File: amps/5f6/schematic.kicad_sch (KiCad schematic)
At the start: 69 parts, among them T3 2R sec

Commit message: Fix: the drawn tone stacks now are the tone stack the lab plots, and a gate says so
The tone-stack lab solves one network — the FMV stack documented in
site/src/lib/tonestack.js — and fills its values from each amp's BOM by
reference designator. Nothing checked that the schematic drew those
designators into that network, and nine of the nine drawings did not.

What the drawings said, rebuilt from the committed .kicad_sch files rather
than from the generators:

- 5F6-A, JTM45, 1987, 1959 and 5F4 ran the treble capacitor off the slope
  resistor's FOOT instead of the stack input, and landed the treble pot's
  lower lug on the bass-capacitor node instead of the slope foot.
- Every three-knob drawing left the bass pot's wiper unwired, so the plotted
  output (treble wiper AND bass wiper) existed on no drawing.
- JTM45, 1987 and 1959 put the mid capacitor in series with the mid pot down
  to ground rather than from the slope foot to the mid leg's top.
- 5F6 tied its bass pot as a rheostat and fed the mid capacitor to the middle
  pot's wiper.
- The blackface circuits left the treble pot's lower lug on the bass-cap node
  and tied the bass wiper to its own lug; AB763 drew its 0.047 µF inline on
  top of the bass pot's lug.

The 5F6-A's own layout.yaml — redrawn from the published Fender 5F6-A layout
sheet — already wires the canonical network (treble low to the slope node,
both wipers to the phase-inverter coupler), and 5F4's does too, so the
drawings were corrected to that rather than the lab to the drawings.

Consequences beyond the wires:

- 5F6-A's parts list prints one 0.02 µF line covering the bass and middle
  positions; the drawing showed one capacitor where the circuit has two.
  Added C5b with the same value and the same printed line cited. The plotted
  curve does not move — both positions already used that value.
- The blackface stacks keep the capacitor that feeds the mid leg. With the
  lug corrected, CBN/CB1 (0.1 µF) feeds the bass pot and CBN2/CB2 (0.047 µ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
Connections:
- net at VR4.3, VR5.1: now also C7.2, VR5.2 (W)
- net at C6.2, VR4.1: no longer VR3.3, VR4.2 (W)
- net at C6.1, C7.1, RSL.2: now also VR3.3
- net at C10.1, VR3.2 (W): now also VR4.2 (W)
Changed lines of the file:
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@@
   (wire (pts (xy 116.84 119.5) (xy 124.46 119.5))
+    (stroke (width 0) (type default)))
+  (junction (at 124.46 119.5) (diameter 0) (color 0 0 0 0))
+  (wire (pts (xy 124.46 119.5) (xy 124.46 94))
+    (stroke (width 0) (type default)))
+  (wire (pts (xy 124.46 94) (xy 140.19 94))
     (stroke (width 0) (type default)))
   (symbol (lib_id "cx:R") (at 128.27 119.5 90) (unit 1)
@@
     (property "Value" "56k" (at 125.07 115.9 270) (effects (font (size 1.27 1.27)) (justify left))))
   (wire (pts (xy 132.08 119.5) (xy 137 119.5))
-    (stroke (width 0) (type default)))
-  (junction (at 121 119.5) (diameter 0) (color 0 0 0 0))
-  (wire (pts (xy 121 119.5) (xy 121 94))
-    (stroke (width 0) (type default)))
-  (wire (pts (xy 121 94) (xy 140.19 94))
     (stroke (width 0) (type default)))
   (symbol (lib_id "cx:C") (at 144 94 90) (unit 1)
@@
     (property "Reference" "VR3" (at 154.6 94.61 0) (effects (font (size 1.27 1.27)) (justify left)))
     (property "Value" "250k treb" (at 154.6 97.01 0) (effects (font (size 1.27 1.27)) (justify left))))
-  (junction (at 137 119.5) (diameter 0) (color 0 0 0 0))
-  (wire (pts (xy 137 119.5) (xy 137 104))
+  (wire (pts (xy 137 119.5) (xy 137 101.62))
     (stroke (width 0) (type default)))
-  (symbol (lib_id "cx:C") (at 144 104 90) (unit 1)
+  (wire (pts (xy 137 101.62) (xy 152.4 101.62))
+    (stroke (width 0) (type default)))
+  (junction (at 137 106) (diameter 0) (color 0 0 0 0))
+  (junction (at 137 118) (diameter 0) (color 0 0 0 0))
+  (symbol (lib_id "cx:C") (at 144 106 90) (unit 1)
     (in_bom yes) (on_board yes)
-    (property "Reference" "C6" (at 140.8 97.8 270) (effects (font (size 1.27 1.27)) (justify left)))
-    (property "Value" ".02u" (at 140.8 100.2 270) (effects (font (size 1.27 1.27)) (justify left))))
-  (wire (pts (xy 137 104) (xy 140.19 104))
+    (property "Reference" "C6" (at 140.8 99.8 270) (effects (font (size 1.27 1.27)) (justify left)))
+    (property "Value" ".02u" (at 140.8 102.2 270) (effects (font (size 1.27 1.27)) (justify left))))
+  (wire (pts (xy 137 106) (xy 140.19 106))
     (stroke (width 0) (type default)))
-  (wire (pts (xy 147.81 104) (xy 152.4 104))
+  (wire (pts (xy 147.81 106) (xy 152.4 106))
     (stroke (width 0) (type default)))
-  (junction (at 152.4 104) (diameter 0) (color 0 0 0 0))
-  (wire (pts (xy 137 119.5) (xy 137 143))
+  (symbol (lib_id "cx:C") (at 144 118 90) (unit 1)
+    (in_bom yes) (on_board yes)
+    (property "Reference" "C7" (at 140.8 111.8 270) (effects (font (size 1.27 1.27)) (justify left)))
+    (property "Value" ".02u" (at 140.8 114.2 270) (effects (font (size 1.27 1.27)) (justify left))))
+  (wire (pts (xy 137 118) (xy 140.19 118))
     (stroke (width 0) (type default)))
-  (symbol (lib_id "cx:C") (at 144 143 90) (unit 1)
-    (in_bom yes) (on_board yes)
-    (property "Reference" "C7" (at 140.8 136.8 270) (effects (font (size 1.27 1.27)) (justify left)))
-    (property "Value" ".02u" (at 140.8 139.2 270) (effects (font (size 1.27 1.27)) (justify left))))
-  (wire (pts (xy 137 143) (xy 140.19 143))
-    (stroke (width 0) (type default)))
-  (wire (pts (xy 147.81 143) (xy 161 143))
-    (stroke (width 0) (type default)))
-  (wire (pts (xy 161 143) (xy 161 121.81))
-    (stroke (width 0) (type default)))
-  (wire (pts (xy 161 121.81) (xy 157.48 121.81))
-    (stroke (width 0) (type default)))
-  (wire (pts (xy 152.4 101.62) (xy 152.4 106))
+  (wire (pts (xy 147.81 118) (xy 152.4 118))
     (stroke (width 0) (type default)))
   (symbol (lib_id "cx:POT") (at 152.4 109.81 0) (unit 1)
@@
     (property "Reference" "VR4" (at 154.6 106.61 0) (effects (font (size 1.27 1.27)) (justify left)))
     (property "Value" "1M bass" (at 154.6 109.01 0) (effects (font (size 1.27 1.27)) (justify left))))
-  (wire (pts (xy 157.48 109.81) (xy 166 109.81))
-    (stroke (width 0) (type default)))
-  (wire (pts (xy 166 109.81) (xy 166 106))
-    (stroke (width 0) (type default)))
-  (wire (pts (xy 166 106) (xy 152.4 106))
-    (stroke (width 0) (type default)))
-  (junction (at 152.4 106) (diameter 0) (color 0 0 0 0))
   (wire (pts (xy 152.4 113.62) (xy 152.4 118))
     (stroke (width 0) (type default)))
+  (junction (at 152.4 118) (diameter 0) (color 0 0 0 0))
   (symbol (lib_id "cx:POT") (at 152.4 121.81 0) (unit 1)
     (in_bom yes) (on_board yes)
     (property "Reference" "VR5" (at 154.6 118.61 0) (effects (font (size 1.27 1.27)) (justify left)))
     (property "Value" "25k mid" (at 154.6 121.01 0) (effects (font (size 1.27 1.27)) (justify left))))
+  (wire (pts (xy 157.48 121.81) (xy 161 121.81))
+    (stroke (width 0) (type default)))
+  (wire (pts (xy 161 121.81) (xy 161 118))
+    (stroke (width 0) (type default)))
+  (wire (pts (xy 161 118) (xy 152.4 118))
+    (stroke (width 0) (type default)))
+  (wire (pts (xy 157.48 109.81) (xy 161 109.81))
+    (stroke (width 0) (type default)))
+  (wire (pts (xy 161 109.81) (xy 161 97.81))
+    (stroke (width 0) (type default)))
+  (wire (pts (xy 161 97.81) (xy 157.48 97.81))
+    (stroke (width 0) (type default)))
+  (junction (at 157.48 97.81) (diameter 0) (color 0 0 0 0))
   (wire (pts (xy 152.4 125.62) (xy 152.4 130))
     (stroke (width 0) (type default)))

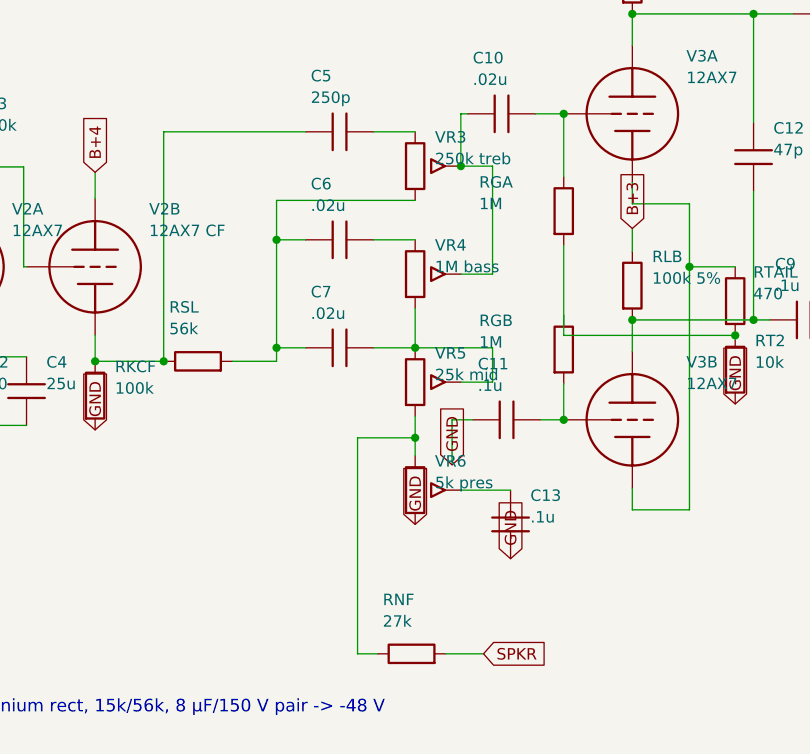
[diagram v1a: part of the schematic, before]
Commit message: Fix: the published sheets draw a different tone stack, and now we draw theirs
The tone-stack pass rewired nine schematics to one "canonical FMV" network —
treble lower lug on the slope foot, treble and bass wipers joined at the
output, mid cap on a rheostat-wired mid pot — on the strength of the 5F6-A
layout.yaml, a redraw that omits the tone capacitors "for legibility" and
whose stack runs were convention, not sheet reading. Fetching the published
drawings and reading them settles what they actually draw, and it is not that
network. Five sheets were read at 300-400 dpi:

- Fender 5F6 (F-EG), schematic AND factory layout pages
- Fender 5F6-A (I-EG), schematic and layout, side by side
- Marshall JTM45 trem ('types 1961, 1962, 1987/T'), Unicord 70-19-11 (1987),
  and the 100 W Type #2 c.1967 (1959)
- Fender Princeton AA964, schematic and factory layout

All of them agree on a ladder: the treble cap and the slope resistor both
leave the stack input; the first bass cap lands on the node shared by the
treble pot's LOWER lug and the bass pot — the treble pot's cold end sits on
the far side of that capacitor, not on the slope foot; the bass pot is a
rheostat (arrow-through-body on most sheets; the JTM45 loops its wiper to the
foot lug, the 5F6 factory layout straps it into the treble-lug node) in
series down the ladder; the mid cap feeds the MIDDLE POT'S WIPER, not its
top; and the stack's output is the treble wiper ALONE. The blackface AA964
draws the same ladder with its 6.8k fixed leg. The 5F6's presence-in-the-
ground-leg arrangement is unchanged and was always right.

So five drawings return to their sheets: 5f6 and aa964 revert to their
pre-rewire wiring (which the extractor confirms matched the sheets all
along), and jtm45/m1987/m1959 are redrawn to the sheets outright — their old
drawings were wrong differently (treble cap off the slope foot, mid cap in
series to ground, bass wiper floating), so neither old nor "canonical" would
do.

The lab keeps all five as prese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
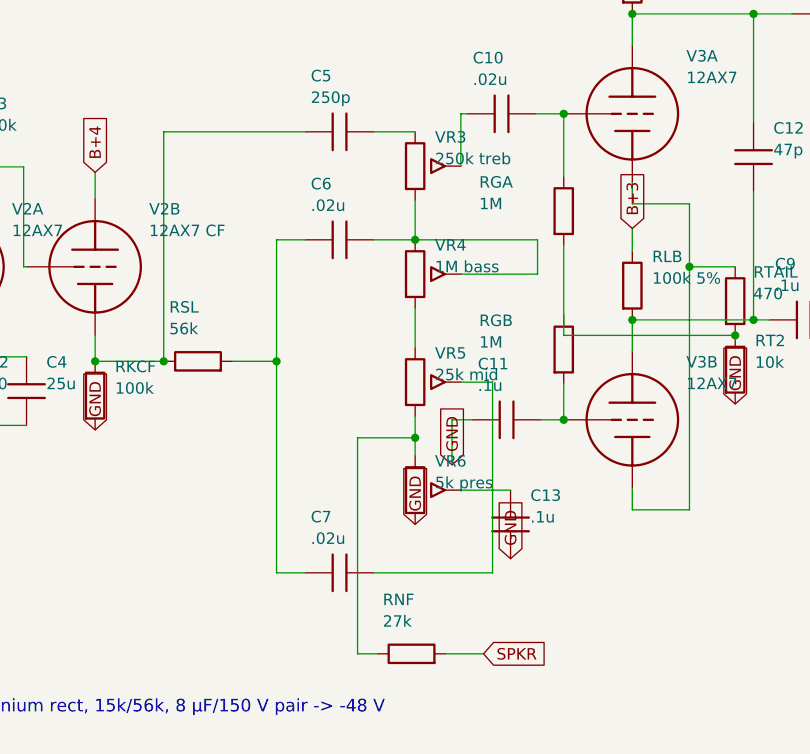
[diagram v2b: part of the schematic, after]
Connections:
- net at C6.1, C7.1, RSL.2: no longer VR3.3
- net at C7.2, VR5.2 (W): no longer VR4.3, VR5.1
- net at C6.2, VR4.1: now also VR3.3, VR4.2 (W)
- net at C10.1, VR3.2 (W): no longer VR4.2 (W)
- new net: VR4.3, VR5.1
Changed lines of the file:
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@@
     (property "Reference" "VR3" (at 154.6 94.61 0) (effects (font (size 1.27 1.27)) (justify left)))
     (property "Value" "250k treb" (at 154.6 97.01 0) (effects (font (size 1.27 1.27)) (justify left))))
-  (wire (pts (xy 137 119.5) (xy 137 101.62))
+  (junction (at 137 119.5) (diameter 0) (color 0 0 0 0))
+  (wire (pts (xy 137 119.5) (xy 137 106))
     (stroke (width 0) (type default)))
-  (wire (pts (xy 137 101.62) (xy 152.4 101.62))
-    (stroke (width 0) (type default)))
-  (junction (at 137 106) (diameter 0) (color 0 0 0 0))
-  (junction (at 137 118) (diameter 0) (color 0 0 0 0))
   (symbol (lib_id "cx:C") (at 144 106 90) (unit 1)
     (in_bom yes) (on_board yes)
@@
   (wire (pts (xy 147.81 106) (xy 152.4 106))
     (stroke (width 0) (type default)))
-  (symbol (lib_id "cx:C") (at 144 118 90) (unit 1)
+  (wire (pts (xy 137 119.5) (xy 137 143))
+    (stroke (width 0) (type default)))
+  (symbol (lib_id "cx:C") (at 144 143 90) (unit 1)
     (in_bom yes) (on_board yes)
-    (property "Reference" "C7" (at 140.8 111.8 270) (effects (font (size 1.27 1.27)) (justify left)))
-    (property "Value" ".02u" (at 140.8 114.2 270) (effects (font (size 1.27 1.27)) (justify left))))
-  (wire (pts (xy 137 118) (xy 140.19 118))
+    (property "Reference" "C7" (at 140.8 136.8 270) (effects (font (size 1.27 1.27)) (justify left)))
+    (property "Value" ".02u" (at 140.8 139.2 270) (effects (font (size 1.27 1.27)) (justify left))))
+  (wire (pts (xy 137 143) (xy 140.19 143))
     (stroke (width 0) (type default)))
-  (wire (pts (xy 147.81 118) (xy 152.4 118))
+  (wire (pts (xy 147.81 143) (xy 161 143))
+    (stroke (width 0) (type default)))
+  (wire (pts (xy 161 143) (xy 161 121.81))
+    (stroke (width 0) (type default)))
+  (wire (pts (xy 161 121.81) (xy 157.48 121.81))
+    (stroke (width 0) (type default)))
+  (wire (pts (xy 152.4 101.62) (xy 152.4 106))
     (stroke (width 0) (type default)))
   (symbol (lib_id "cx:POT") (at 152.4 109.81 0) (unit 1)
@@
     (property "Reference" "VR4" (at 154.6 106.61 0) (effects (font (size 1.27 1.27)) (justify left)))
     (property "Value" "1M bass" (at 154.6 109.01 0) (effects (font (size 1.27 1.27)) (justify left))))
+  (wire (pts (xy 157.48 109.81) (xy 166 109.81))
+    (stroke (width 0) (type default)))
+  (wire (pts (xy 166 109.81) (xy 166 106))
+    (stroke (width 0) (type default)))
+  (wire (pts (xy 166 106) (xy 152.4 106))
+    (stroke (width 0) (type default)))
+  (junction (at 152.4 106) (diameter 0) (color 0 0 0 0))
   (wire (pts (xy 152.4 113.62) (xy 152.4 118))
     (stroke (width 0) (type default)))
-  (junction (at 152.4 118) (diameter 0) (color 0 0 0 0))
   (symbol (lib_id "cx:POT") (at 152.4 121.81 0) (unit 1)
     (in_bom yes) (on_board yes)
     (property "Reference" "VR5" (at 154.6 118.61 0) (effects (font (size 1.27 1.27)) (justify left)))
     (property "Value" "25k mid" (at 154.6 121.01 0) (effects (font (size 1.27 1.27)) (justify left))))
-  (wire (pts (xy 157.48 121.81) (xy 161 121.81))
-    (stroke (width 0) (type default)))
-  (wire (pts (xy 161 121.81) (xy 161 118))
-    (stroke (width 0) (type default)))
-  (wire (pts (xy 161 118) (xy 152.4 118))
-    (stroke (width 0) (type default)))
-  (wire (pts (xy 157.48 109.81) (xy 161 109.81))
-    (stroke (width 0) (type default)))
-  (wire (pts (xy 161 109.81) (xy 161 97.81))
-    (stroke (width 0) (type default)))
-  (wire (pts (xy 161 97.81) (xy 157.48 97.81))
-    (stroke (width 0) (type default)))
-  (junction (at 157.48 97.81) (diameter 0) (color 0 0 0 0))
   (wire (pts (xy 152.4 125.62) (xy 152.4 130))
     (stroke (width 0) (type default)))

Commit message: Fix: one lettering convention per surface, engine-enforced; legend inside the viewBox
WS3 — layout pipeline + cross-surface value-consistency engine.

## One convention per surface (docs/lettering-conventions.md, new)

The same part stated its value in several notations at once. 5E3 C6 and 5D3 C6
rendered "5n" on the schematic, "0.005 µF · 600 V" in the parts list and
"0.005 µF" on the board. 5F6-A RD1 printed "4,700 Ω" beside neighbours printing
"15 kΩ". check_value_consistency proves the surfaces name the same QUANTITY; it
cannot see that they name it three ways. So each surface now has exactly one
convention and every one of them is gated:

* house units in bom.yaml/prose — engineering prefix with the mantissa 1…999,
  pF below 1000 pF and µF at and above it, no comma-grouped thousands. 19 values
  normalised (5E6-A, 5F6-A, 5F10, 6161, 6G2, 6G5, 6G6-B).
* schematic drafting shorthand — the unit letter is the SI prefix of the house
  unit, in the amp's declared idiom (meta.yaml conventions.notation: us|uk).
  British RKM/nanofarad practice on the Hiwatt and the 2204 is DECLARED, not
  normalised away; it is what those source drawings letter. Secondary ratings
  are space-separated fields with their own unit ("20u 600V"), never the era's
  dashed shorthand and never the house middot. 30 symbol values corrected across
  ten draw scripts.
* era sheet lettering — generated only, by era_pair(); documented cases and a
  corpus round-trip sweep in test_era_values.py, now 57 cases.

## Era-lettering fall-throughs closed

A value era_pair() refuses came back as the house string, and a house string can
be a whole sentence. Fixed at the source rather than per case:

* body_value() — a parenthetical GLOSS is never lettered on a component body.
  "selenium (silicon diode in modern builds)" was lettered in full on the 5E4-A
  and ran off the left edge of the page.
* twin cans letter as the era sheets did: 25 µF + 25 µF -> "25/25MFD".
* a repeat count is not a rating: "(×2)" com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
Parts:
- RGS1, RGS2: value 1500 -> 1.5k
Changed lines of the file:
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@@
     (in_bom yes) (on_board yes)
     (property "Reference" "RGS1" (at 207.8 78 270) (effects (font (size 1.27 1.27)) (justify left)))
-    (property "Value" "1500" (at 207.8 80.4 270) (effects (font (size 1.27 1.27)) (justify left))))
+    (property "Value" "1.5k" (at 207.8 80.4 270) (effects (font (size 1.27 1.27)) (justify left))))
   (wire (pts (xy 205.74 84) (xy 207.19 84))
     (stroke (width 0) (type default)))
@@
     (in_bom yes) (on_board yes)
     (property "Reference" "RGS2" (at 207.8 130 270) (effects (font (size 1.27 1.27)) (justify left)))
-    (property "Value" "1500" (at 207.8 132.4 270) (effects (font (size 1.27 1.27)) (justify left))))
+    (property "Value" "1.5k" (at 207.8 132.4 270) (effects (font (size 1.27 1.27)) (justify left))))
   (wire (pts (xy 205.74 136) (xy 207.19 136))
     (stroke (width 0) (type default)))
